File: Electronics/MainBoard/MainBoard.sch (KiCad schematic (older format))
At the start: 27 parts, among them CN3 RCable_Con_VEST, J1 CONN_02X04, M1 Vibr_Motor, Q1 Q_PNP_CBE, SW1 SW_PUSH, SW2 SPST

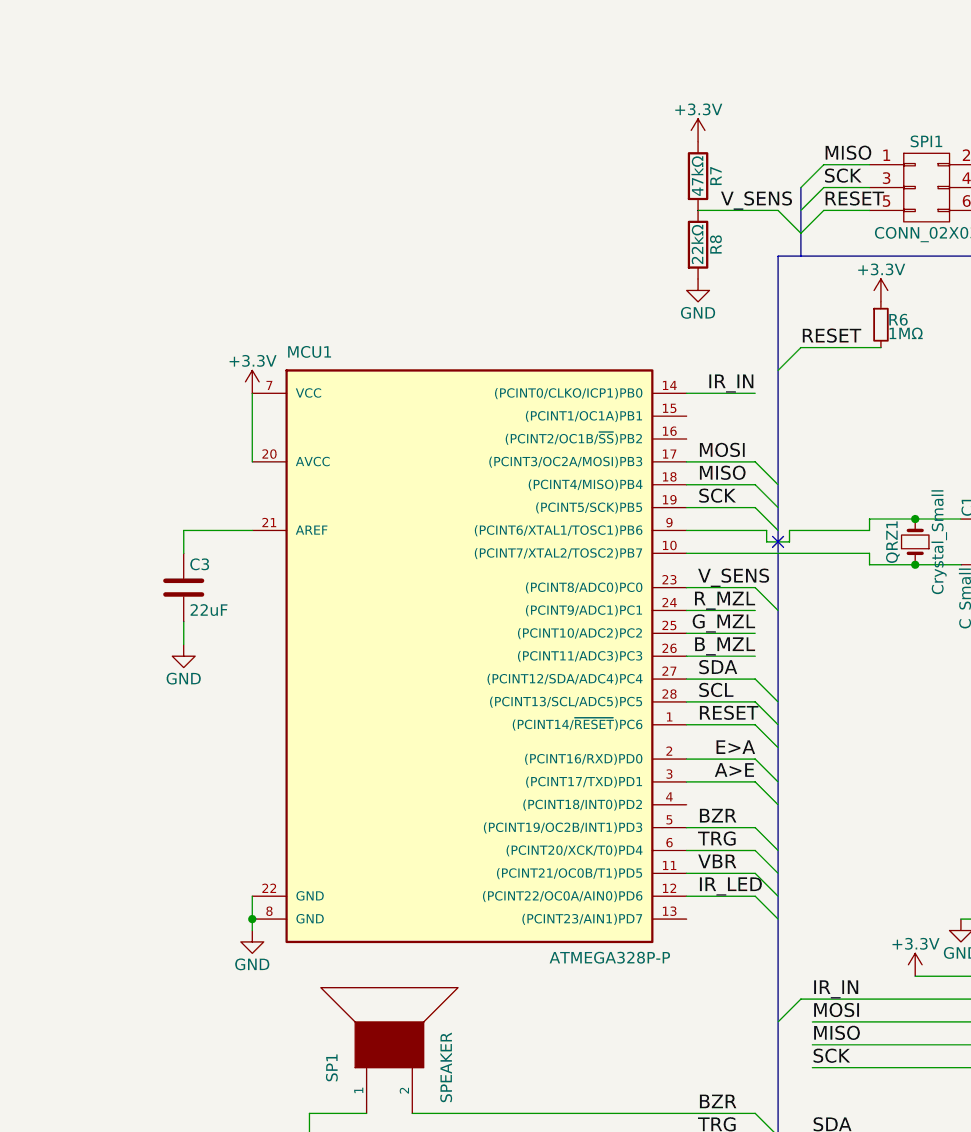
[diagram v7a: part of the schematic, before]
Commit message: First implement of SMD components
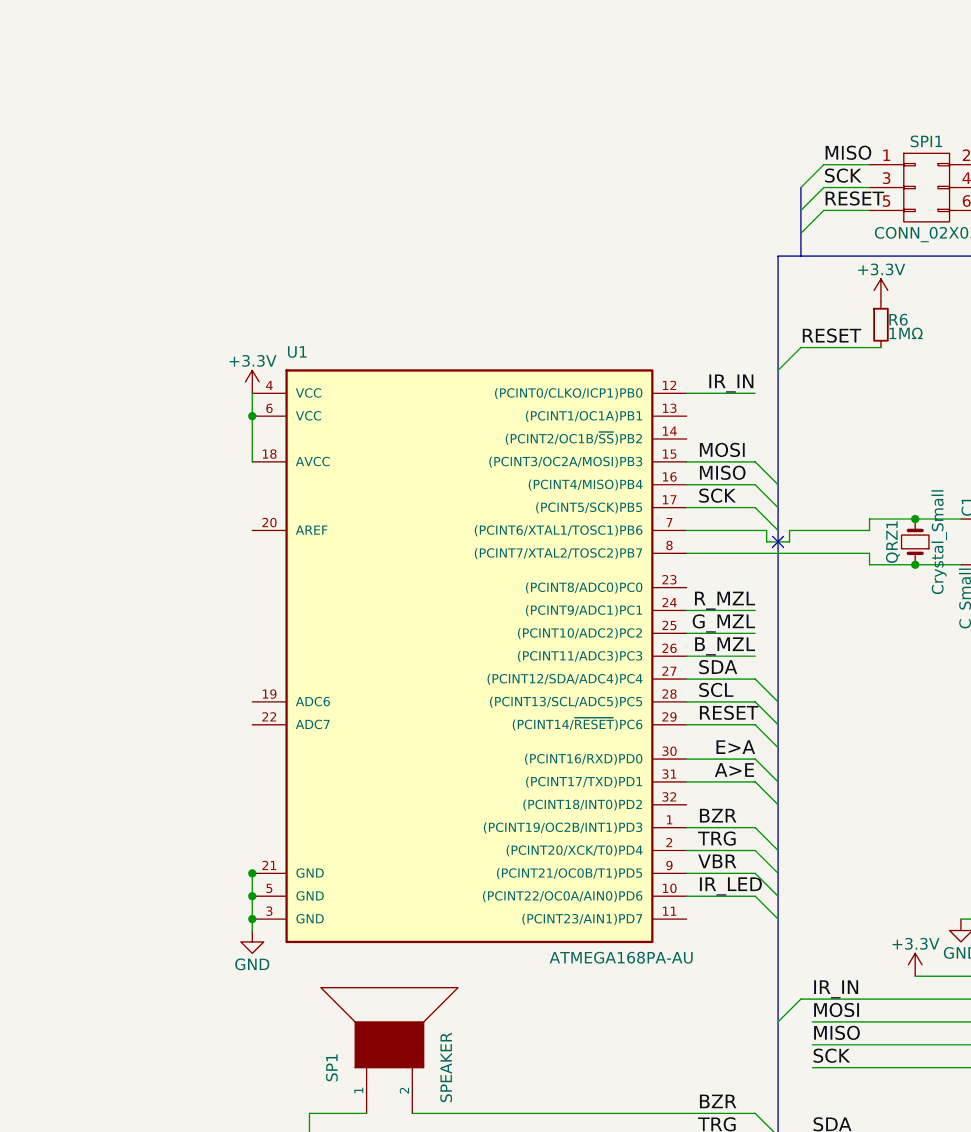
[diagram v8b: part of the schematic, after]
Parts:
- removed C3: 22uF, Capacitors_ThroughHole:CP_Radial_D5.0mm_P2.50mm, symbol C
- removed MCU1: ATMEGA328P-P, Housings_DIP:DIP-28_W7.62mm, symbol ATMEGA328P-P
- removed R7: 47kΩ, Discret:R1, symbol R
- removed R8: 22kΩ, Discret:R1, symbol R
- added U1: ATMEGA168PA-AU, Housings_QFP:TQFP-32_7x7mm_Pitch0.8mm, symbol ATMEGA168PA-AU
- C1, C2: footprint Capacitors_ThroughHole:C_Disc_D3_P2.5 -> Capacitors_SMD:C_0603_HandSoldering
- R1, R11, R9: footprint Resistors_ThroughHole:R_Axial_DIN0204_L3.6mm_D1.6mm_P2.54mm_Vertical -> Resistors_SMD:R_0603_HandSoldering
- R3, R4, R5, R6: footprint Discret:R1 -> Resistors_SMD:R_0603_HandSoldering
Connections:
- net +3V3: now also U1.18 (AVCC), U1.4 (VCC), U1.6 (VCC)
- net A>E: now also U1.31 ((PCINT17/TXD)PD1)
- net BZR: now also U1.1 ((PCINT19/OC2B/INT1)PD3)
- net B_MZL: now also U1.26 ((PCINT11/ADC3)PC3)
- net E>A: now also U1.30 ((PCINT16/RXD)PD0)
- net GND: now also U1.21 (GND), U1.3 (GND), U1.5 (GND)
- net G_MZL: now also U1.25 ((PCINT10/ADC2)PC2)
- net IR_IN: now also U1.12 ((PCINT0/CLKO/ICP1)PB0)
- net IR_LED: now also U1.10 ((PCINT22/OC0A/AIN0)PD6)
- net MISO: now also U1.16 ((PCINT4/MISO)PB4)
- net MOSI: now also U1.15 ((PCINT3/OC2A/MOSI)PB3)
- net RESET: now also U1.29 ((PCINT14/~RESET~)PC6)
- net R_MZL: now also U1.24 ((PCINT9/ADC1)PC1)
- net SCK: now also U1.17 ((PCINT5/SCK)PB5)
- net SCL: now also U1.28 ((PCINT13/SCL/ADC5)PC5)
- net SDA: now also U1.27 ((PCINT12/SDA/ADC4)PC4)
- net TRG: now also U1.2 ((PCINT20/XCK/T0)PD4)
- net VBR: now also U1.9 ((PCINT21/OC0B/T1)PD5)
- net at C2.2, QRZ1.1: now also U1.8 ((PCINT7/XTAL2/TOSC2)PB7)
- net at C1.1, QRZ1.2: now also U1.7 ((PCINT6/XTAL1/TOSC1)PB6)
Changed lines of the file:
@@
 $EndDescr
-$Comp
-L ATMEGA328P-P MCU1
-U 1 1 572B3530
-P 6100 3550
-F 0 "MCU1" H 5350 4800 50  0000 L BNN
-F 1 "ATMEGA328P-P" H 6500 2150 50  0000 L BNN
-F 2 "Housings_DIP:DIP-28_W7.62mm" H 6100 3550 50  0001 C CIN
-F 3 "" H 6100 3550 50  0000 C CNN
-	1    6100 3550
-	1    0    0    -1
-$EndComp
 $Comp
 L Crystal_Small QRZ1
@@
 F 0 "C1" H 8410 3070 50  0000 L CNN
 F 1 "C_Small" H 8410 2920 50  0000 L CNN
-F 2 "Capacitors_ThroughHole:C_Disc_D3_P2.5" H 8400 3000 50  0001 C CNN
+F 2 "Capacitors_SMD:C_0603_HandSoldering" H 8400 3000 50  0001 C CNN
 F 3 "" H 8400 3000 50  0000 C CNN
 	1    8400 3000
@@
 F 0 "C2" H 8410 3270 50  0000 L CNN
 F 1 "C_Small" H 8410 3120 50  0000 L CNN
-F 2 "Capacitors_ThroughHole:C_Disc_D3_P2.5" H 8400 3200 50  0001 C CNN
+F 2 "Capacitors_SMD:C_0603_HandSoldering" H 8400 3200 50  0001 C CNN
 F 3 "" H 8400 3200 50  0000 C CNN
 	1    8400 3200
@@
 	8550 3200 8550 3300
 $Comp
-L GND #PWR01
+L GND #PWR12
 U 1 1 572B3BB9
 P 8550 3300
-F 0 "#PWR01" H 8550 3050 50  0001 C CNN
+F 0 "#PWR12" H 8550 3050 50  0001 C CNN
 F 1 "GND" H 8550 3150 50  0000 C CNN
 F 2 "" H 8550 3300 50  0000 C CNN
@@
 Connection ~ 8100 3200
 $Comp
-L GND #PWR02
+L GND #PWR5
 U 1 1 572B3ED7
 P 5200 4800
-F 0 "#PWR02" H 5200 4550 50  0001 C CNN
+F 0 "#PWR5" H 5200 4550 50  0001 C CNN
 F 1 "GND" H 5200 4650 50  0000 C CNN
 F 2 "" H 5200 4800 50  0000 C CNN
@@
 $EndComp
 Wire Wire Line
-	5200 4650 5200 4800
+	5200 4550 5200 4800
 Connection ~ 5200 4750
-Wire Wire Line
-	4900 3050 5200 3050
 Wire Wire Line
 	5200 2750 5200 2450
@@
 $EndComp
 $Comp
-L GND #PWR03
+L GND #PWR16
 U 1 1 572B59E3
 P 10250 5850
-F 0 "#PWR03" H 10250 5600 50  0001 C CNN
+F 0 "#PWR16" H 10250 5600 50  0001 C CNN
 F 1 "GND" H 10250 5700 50  0000 C CNN
 F 2 "" H 10250 5850 50  0000 C CNN
@@
 	1    0    0    -1
 $EndComp
-Wire Wire Line
-	7100 3300 7400 3300
 $Comp
 L CONN_02X03 SPI1
@@
 $EndComp
 $Comp
-L +3.3V #PWR04
+L +3.3V #PWR10
 U 1 1 572B6CF2
 P 8500 1450
-F 0 "#PWR04" H 8500 1300 50  0001 C CNN
+F 0 "#PWR10" H 8500 1300 50  0001 C CNN
 F 1 "+3.3V" H 8500 1590 50  0000 C CNN
 F 2 "" H 8500 1450 50  0000 C CNN
@@
 $EndComp
 $Comp
-L +3.3V #PWR05
+L +3.3V #PWR15
 U 1 1 572B6F24
 P 10250 4250
-F 0 "#PWR05" H 10250 4100 50  0001 C CNN
+F 0 "#PWR15" H 10250 4100 50  0001 C CNN
 F 1 "+3.3V" H 10250 4390 50  0000 C CNN
 F 2 "" H 10250 4250 50  0000 C CNN
@@
 $EndComp
 $Comp
-L +3.3V #PWR06
+L +3.3V #PWR4
 U 1 1 572B7083
 P 5200 2450
-F 0 "#PWR06" H 5200 2300 50  0001 C CNN
+F 0 "#PWR4" H 5200 2300 50  0001 C CNN
 F 1 "+3.3V" H 5200 2590 50  0000 C CNN
 F 2 "" H 5200 2450 50  0000 C CNN
@@
 F 0 "R3" V 2850 3525 50  0000 L CNN
 F 1 "220Ω" V 2725 3625 50  0000 L CNN
-F 2 "Discret:R1" H 2800 3700 50  0001 C CNN
+F 2 "Resistors_SMD:R_0603_HandSoldering" H 2800 3700 50  0001 C CNN
 F 3 "" H 2800 3700 50  0000 C CNN
 	1    2800 3700
@@
 F 0 "R4" V 2850 3725 50  0000 L CNN
 F 1 "220Ω" V 2725 3825 50  0000 L CNN
-F 2 "Discret:R1" H 2800 3900 50  0001 C CNN
+F 2 "Resistors_SMD:R_0603_HandSoldering" H 2800 3900 50  0001 C CNN
 F 3 "" H 2800 3900 50  0000 C CNN
 	1    2800 3900
@@
 F 0 "R5" V 2850 3925 50  0000 L CNN
 F 1 "220Ω" V 2725 4025 50  0000 L CNN
-F 2 "Discret:R1" H 2800 4100 50  0001 C CNN
+F 2 "Resistors_SMD:R_0603_HandSoldering" H 2800 4100 50  0001 C CNN
 F 3 "" H 2800 4100 50  0000 C CNN
 	1    2800 4100
@@
 F 0 "R6" H 7980 2170 50  0000 L CNN
 F 1 "1MΩ" H 7980 2110 50  0000 L CNN
-F 2 "Discret:R1" H 7950 2150 50  0001 C CNN
+F 2 "Resistors_SMD:R_0603_HandSoldering" H 7950 2150 50  0001 C CNN
 F 3 "" H 7950 2150 50  0000 C CNN
 	1    7950 2150
@@
 $EndComp
 $Comp
-L +3.3V #PWR07
+L +3.3V #PWR7
 U 1 1 572DCEA7
 P 7950 2050
-F 0 "#PWR07" H 7950 1900 50  0001 C CNN
+F 0 "#PWR7" H 7950 1900 50  0001 C CNN
 F 1 "+3.3V" H 7950 2190 50  0000 C CNN
 F 2 "" H 7950 2050 50  0000 C CNN
@@
 Entry Wire Line
 	7400 4150 7500 4250
-Entry Wire Line
-	7400 3300 7500 3400
-Text Label 7150 3300 0    60   ~ 0
-V_SENS
-$Comp
-L R R7
-U 1 1 572CF4CC
-P 7150 1500
-F 0 "R7" V 7230 1500 50  0000 C CNN
-F 1 "47kΩ" V 7150 1500 50  0000 C CNN
-F 2 "Discret:R1" V 7080 1500 50  0001 C CNN
-F 3 "" H 7150 1500 50  0000 C CNN
-	1    7150 1500
-	1    0    0    -1
-$EndComp
-$Comp
-L R R8
-U 1 1 572CF50F
-P 7150 1800
-F 0 "R8" V 7230 1800 50  0000 C CNN
-F 1 "22kΩ" V 7150 1800 50  0000 C CNN
-F 2 "Discret:R1" V 7080 1800 50  0001 C CNN
-F 3 "" H 7150 1800 50  0000 C CNN
-	1    7150 1800
-	1    0    0    -1
-$EndComp
-$Comp
-L GND #PWR08
-U 1 1 572CF9FB
-P 7150 1950
-F 0 "#PWR08" H 7150 1700 50  0001 C CNN
-F 1 "GND" H 7150 1800 50  0000 C CNN
-F 2 "" H 7150 1950 50  0000 C CNN
-F 3 "" H 7150 1950 50  0000 C CNN
-	1    7150 1950
-	1    0    0    -1
-$EndComp
-$Comp
-L +3.3V #PWR09
-U 1 1 572CFBB3
-P 7150 1350
-F 0 "#PWR09" H 7150 1200 50  0001 C CNN
-F 1 "+3.3V" H 7150 1490 50  0000 C CNN
-F 2 "" H 7150 1350 50  0000 C CNN
-F 3 "" H 7150 1350 50  0000 C CNN
-	1    7150 1350
-	1    0    0    -1
-$EndComp
-Wire Wire Line
-	7150 1650 7500 1650
-Entry Wire Line
-	7500 1650 7600 1750
-Text Label 7250 1650 0    60   ~ 0
-V_SENS
 Wire Wire Line
 	7100 4350 7400 4350
@@
 SCL
 $Comp
-L GND #PWR010
+L GND #PWR9
 U 1 1 572D931B
 P 8300 4750
-F 0 "#PWR010" H 8300 4500 50  0001 C CNN
+F 0 "#PWR9" H 8300 4500 50  0001 C CNN
 F 1 "GND" H 8300 4600 50  0000 C CNN
 F 2 "" H 8300 4750 50  0000 C CNN
@@
 	8400 4750 8300 4750
 $Comp
-L +3.3V #PWR011
+L +3.3V #PWR8
 U 1 1 572D98DD
 P 8100 5000
-F 0 "#PWR011" H 8100 4850 50  0001 C CNN
+F 0 "#PWR8" H 8100 4850 50  0001 C CNN
 F 1 "+3.3V" H 8100 5140 50  0000 C CNN
 F 2 "" H 8100 5000 50  0000 C CNN
@@
 Connection ~ 5450 6350
 $Comp
-L GND #PWR012
+L GND #PWR6
 U 1 1 572E5080
 P 5450 6400
-F 0 "#PWR012" H 5450 6150 50  0001 C CNN
+F 0 "#PWR6" H 5450 6150 50  0001 C CNN
 F 1 "GND" H 5450 6250 50  0000 C CNN
 F 2 "" H 5450 6400 50  0000 C CNN
@@
 VBR
 $Comp
-L GND #PWR013
+L GND #PWR11
 U 1 1 572EF82E
 P 8500 1650
-F 0 "#PWR013" H 8500 1400 50  0001 C CNN
+F 0 "#PWR11" H 8500 1400 50  0001 C CNN
 F 1 "GND" H 8500 1500 50  0000 C CNN
 F 2 "" H 8500 1650 50  0000 C CNN
@@
 	9700 1800 9700 1950
 $Comp
-L +3.3V #PWR014
+L +3.3V #PWR13
 U 1 1 595AF7EE
 P 9400 1000
-F 0 "#PWR014" H 9400 850 50  0001 C CNN
+F 0 "#PWR13" H 9400 850 50  0001 C CNN
 F 1 "+3.3V" H 9400 1140 50  0000 C CNN
 F 2 "" H 9400 1000 50  0001 C CNN
@@
 F 0 "R9" H 9530 1120 50  0001 L CNN
 F 1 "RST" H 9530 1060 50  0001 L CNN
-F 2 "Resistors_ThroughHole:R_Axial_DIN0204_L3.6mm_D1.6mm_P2.54mm_Vertical" H 9500 1100 50  0001 C CNN
+F 2 "Resistors_SMD:R_0603_HandSoldering" H 9500 1100 50  0001 C CNN
 F 3 "" H 9500 1100 50  0001 C CNN
 	1    9500 1100
@@
 	9400 1000 9600 1000
 $Comp
-L GND #PWR015
+L GND #PWR14
 U 1 1 595B47CF
 P 9700 1950
-F 0 "#PWR015" H 9700 1700 50  0001 C CNN
+F 0 "#PWR14" H 9700 1700 50  0001 C CNN
 F 1 "GND" H 9700 1800 50  0000 C CNN
 F 2 "" H 9700 1950 50  0001 C CNN
@@
 F 0 "R11" H 9630 1120 50  0001 L CNN
 F 1 "RST" H 9630 1060 50  0001 L CNN
-F 2 "Resistors_ThroughHole:R_Axial_DIN0204_L3.6mm_D1.6mm_P2.54mm_Vertical" H 9600 1100 50  0001 C CNN
+F 2 "Resistors_SMD:R_0603_HandSoldering" H 9600 1100 50  0001 C CNN
 F 3 "" H 9600 1100 50  0001 C CNN
 	1    9600 1100
@@
 $EndComp
 Connection ~ 9500 1000
-$Comp
-L C C3
-U 1 1 595C0FD8
-P 4900 3300
-F 0 "C3" H 4925 3400 50  0000 L CNN
-F 1 "22uF" H 4925 3200 50  0000 L CNN
-F 2 "Capacitors_ThroughHole:CP_Radial_D5.0mm_P2.50mm" H 4938 3150 50  0001 C CNN
-F 3 "" H 4900 3300 50  0001 C CNN
-	1    4900 3300
-	1    0    0    -1
-$EndComp
-Wire Wire Line
-	4900 3050 4900 3150
-Wire Wire Line
-	4900 3450 4900 3550
-$Comp
-L GND #PWR016
-U 1 1 595C115B
-P 4900 3550
-F 0 "#PWR016" H 4900 3300 50  0001 C CNN
-F 1 "GND" H 4900 3400 50  0000 C CNN
-F 2 "" H 4900 3550 50  0001 C CNN
-F 3 "" H 4900 3550 50  0001 C CNN
-	1    4900 3550
-	1    0    0    -1
-$EndComp
 Wire Wire Line
 	7100 3400 7400 3400
@@
 	2000 2550 2000 2800
 $Comp
-L +3.3V #PWR017
+L +3.3V #PWR1
 U 1 1 596FE8E8
 P 2000 2550
-F 0 "#PWR017" H 2000 2400 50  0001 C CNN
+F 0 "#PWR1" H 2000 2400 50  0001 C CNN
 F 1 "+3.3V" H 2000 2690 50  0000 C CNN
 F 2 "" H 2000 2550 50  0001 C CNN
@@
 Connection ~ 2000 3650
 $Comp
-L GND #PWR018
+L GND #PWR2
 U 1 1 59700916
 P 2000 4200
-F 0 "#PWR018" H 2000 3950 50  0001 C CNN
+F 0 "#PWR2" H 2000 3950 50  0001 C CNN
 F 1 "GND" H 2000 4050 50  0000 C CNN
 F 2 "" H 2000 4200 50  0001 C CNN
@@
 F 0 "R1" V 2530 3400 50  0000 C CNN
 F 1 "220Ω" V 2450 3400 50  0000 C CNN
-F 2 "Resistors_ThroughHole:R_Axial_DIN0204_L3.6mm_D1.6mm_P2.54mm_Vertical" V 2380 3400 50  0001 C CNN
+F 2 "Resistors_SMD:R_0603_HandSoldering" V 2380 3400 50  0001 C CNN
 F 3 "" H 2450 3400 50  0001 C CNN
 	1    2450 3400
@@
 Wire Wire Line
 	8400 5400 7650 5400
+$Comp
+L ATMEGA168PA-AU U1
+U 1 1 5A719FA4
+P 6100 3550
+F 0 "U1" H 5350 4800 50  0000 L BNN
+F 1 "ATMEGA168PA-AU" H 6500 2150 50  0000 L BNN
+F 2 "Housings_QFP:TQFP-32_7x7mm_Pitch0.8mm" H 6100 3550 50  0001 C CIN
+F 3 "" H 6100 3550 50  0001 C CNN
+	1    6100 3550
+	1    0    0    -1
+$EndComp
+Connection ~ 5200 4650
+Connection ~ 5200 4550
+Connection ~ 5200 2550
 $EndSCHEMATC
